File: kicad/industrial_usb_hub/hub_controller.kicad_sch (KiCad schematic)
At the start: 36 parts, among them U1 USB5744-I_2G, Y1 Crystal_GND24

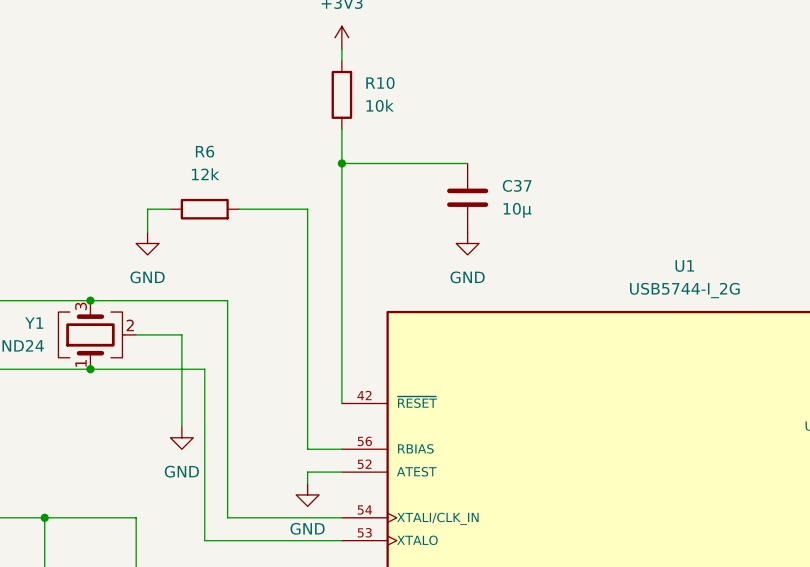
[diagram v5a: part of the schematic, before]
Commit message: added testpoints
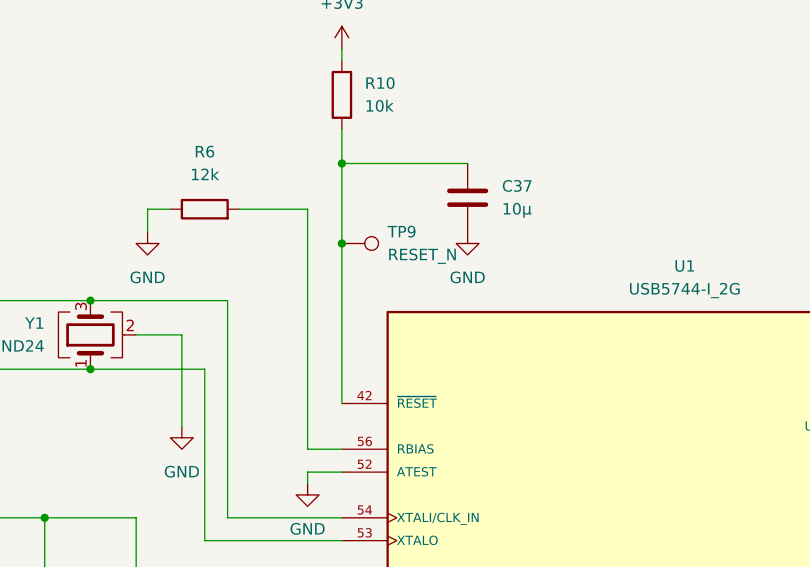
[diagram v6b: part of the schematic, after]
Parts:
- added TP9: RESET_N, TestPoint:TestPoint_Pad_1.0x1.0mm, symbol Connector:TestPoint
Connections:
- net at C37.2, R10.1, U1.42 (~{RESET}): now also TP9.1
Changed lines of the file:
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@@
 	)
 	(junction
+		(at 104.14 44.45)
+		(diameter 0)
+		(color 0 0 0 0)
+	)
+	(junction
 		(at 224.79 57.15)
 		(diameter 0)
@@
 	(wire
 		(pts
-			(xy 104.14 35.56) (xy 104.14 62.23)
+			(xy 104.14 35.56) (xy 104.14 44.45)
 		)
 		(stroke
@@
 	(wire
 		(pts
+			(xy 104.14 44.45) (xy 104.14 62.23)
+		)
+		(stroke
+			(width 0)
+			(type default)
+		)
+	)
+	(wire
+		(pts
 			(xy 247.65 40.64) (xy 251.46 40.64)
 		)
@@
 					(unit 1)
 				)
+			)
+		)
+	)
+	(symbol
+		(lib_id "Connector:TestPoint")
+		(at 104.14 44.45 270)
+		(unit 1)
+		(exclude_from_sim no)
+		(in_bom yes)
+		(on_board yes)
+		(dnp no)
+		(fields_autoplaced yes)
+		(property "Reference" "TP9"
+			(at 109.22 43.1799 90)
+			(effects
+				(font
+					(size 1.27 1.27)
+				)
+				(justify left)
+			)
+		)
+		(property "Value" "RESET_N"
+			(at 109.22 45.7199 90)
+			(effects
+				(font
+					(size 1.27 1.27)
+				)
+				(justify left)
+			)
+		)
+		(property "Footprint" "TestPoint:TestPoint_Pad_1.0x1.0mm"
+			(at 104.14 49.53 0)
+			(effects
+				(font
+					(size 1.27 1.27)
+				)
+				(hide yes)
+			)
+		)
+		(property "Datasheet" "~"
+			(at 104.14 49.53 0)
+			(effects
+				(font
+					(size 1.27 1.27)
+				)
+				(hide yes)
+			)
+		)
+		(property "Description" "test point"
+			(at 104.14 44.45 0)
+			(effects
+				(font
+					(size 1.27 1.27)
+				)
+				(hide yes)
+			)
+		)
+		(pin "1"
+		)
+		(instances
+			(project "industrial_usb_hub"
+				(path "/2bdf928d-3bff-4ef5-bf26-63be25952cbb/b4bd7b8c-79d1-41e8-9458-60ff5f44690b"
+					(reference "TP9")
+					(unit 1)
+				)
